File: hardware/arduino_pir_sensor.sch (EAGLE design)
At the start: 43 parts, among them U2 TPS61097-33, U3 BISS0001SO16, U4 NRF24L01+_MODULE, U5 D203S

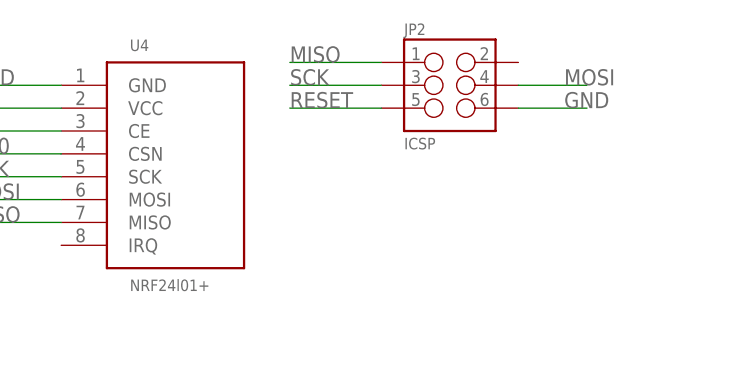
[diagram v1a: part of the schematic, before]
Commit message: - cutout in ground planes on all PCB layers added below wireless module antenna - serial communication connector added
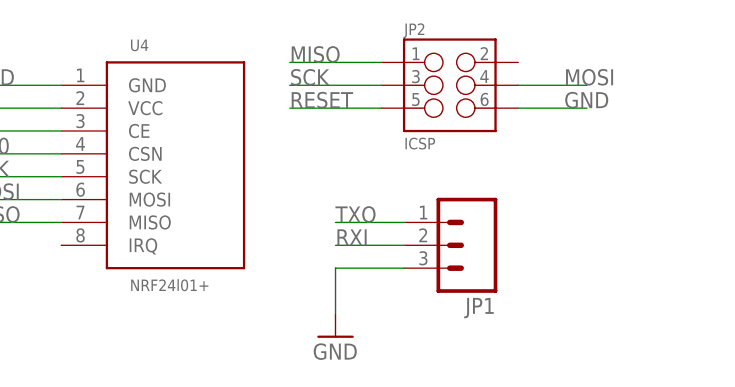
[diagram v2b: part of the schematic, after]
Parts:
- added JP1: (no value), endy-connectors:M03PTH
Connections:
- net GND: now also JP1.3
- net RXI: now also JP1.2
- net TXO: now also JP1.1
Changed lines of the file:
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@@
 <part name="P+8" library="SparkFun" deviceset="3.3V" device="" value="VCC"/>
 <part name="FRAME1" library="SparkFun-Aesthetics" deviceset="FRAME-A3" device=""/>
+<part name="JP1" library="endy-connectors" deviceset="M03" device="PTH"/>
+<part name="GND20" library="SparkFun" deviceset="GND" device=""/>
 </parts>
 <sheets>
@@
 <instance part="P+8" gate="G$1" x="63.5" y="162.56"/>
 <instance part="FRAME1" gate="G$1" x="-142.24" y="-68.58"/>
+<instance part="JP1" gate="G$1" x="185.42" y="17.78" rot="R180"/>
+<instance part="GND20" gate="1" x="170.18" y="7.62"/>
 </instances>
 <busses>
@@
 <pinref part="C16" gate="G$1" pin="P$2"/>
 <wire x1="63.5" y1="142.24" x2="63.5" y2="147.32" width="0.1524" layer="91"/>
+</segment>
+<segment>
+<pinref part="JP1" gate="G$1" pin="3"/>
+<pinref part="GND20" gate="1" pin="GND"/>
+<wire x1="177.8" y1="15.24" x2="170.18" y2="15.24" width="0.1524" layer="91"/>
+<wire x1="170.18" y1="15.24" x2="170.18" y2="10.16" width="0.1524" layer="91"/>
 </segment>
 </net>
@@
 <pinref part="U1" gate="G$1" pin="PD1(TXD)"/>
 </segment>
+<segment>
+<pinref part="JP1" gate="G$1" pin="1"/>
+<wire x1="177.8" y1="20.32" x2="170.18" y2="20.32" width="0.1524" layer="91"/>
+<label x="170.18" y="20.32" size="1.778" layer="95"/>
+</segment>
 </net>
 <net name="D9" class="0">
@@
 <pinref part="U1" gate="G$1" pin="PD0(RXD)"/>
 </segment>
-</net>
+<segment>
+<pinref part="JP1" gate="G$1" pin="2"/>
+<wire x1="177.8" y1="17.78" x2="170.18" y2="17.78" width="0.1524" layer="91"/>
+<label x="170.18" y="17.78" size="1.778" layer="95"/>
+</segment>
+</net>

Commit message: - schematic pdf file updated
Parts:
- JP1: value (none) -> Serial
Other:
- moved on the sheet: JP1, JP2
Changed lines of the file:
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@@
 <part name="P+8" library="SparkFun" deviceset="3.3V" device="" value="VCC"/>
 <part name="FRAME1" library="SparkFun-Aesthetics" deviceset="FRAME-A3" device=""/>
-<part name="JP1" library="endy-connectors" deviceset="M03" device="PTH"/>
+<part name="JP1" library="endy-connectors" deviceset="M03" device="PTH" value="Serial"/>
 <part name="GND20" library="SparkFun" deviceset="GND" device=""/>
 </parts>
@@
 </instance>
 <instance part="P+3" gate="G$1" x="91.44" y="134.62"/>
-<instance part="JP2" gate="G$1" x="182.88" y="35.56">
-<attribute name="OC_NEWARK" x="182.88" y="35.56" size="1.778" layer="96" display="off"/>
-<attribute name="MF" x="182.88" y="35.56" size="1.778" layer="96" display="off"/>
-<attribute name="MPN" x="182.88" y="35.56" size="1.778" layer="96" display="off"/>
+<instance part="JP2" gate="G$1" x="195.58" y="33.02" smashed="yes">
+<attribute name="OC_NEWARK" x="195.58" y="33.02" size="1.778" layer="96" display="off"/>
+<attribute name="MF" x="195.58" y="33.02" size="1.778" layer="96" display="off"/>
+<attribute name="MPN" x="195.58" y="33.02" size="1.778" layer="96" display="off"/>
+<attribute name="NAME" x="190.5" y="38.608" size="1.27" layer="95"/>
+<attribute name="VALUE" x="190.5" y="25.908" size="1.27" layer="96"/>
 </instance>
 <instance part="C2" gate="G$1" x="93.98" y="63.5">
@@
 <instance part="P+8" gate="G$1" x="63.5" y="162.56"/>
 <instance part="FRAME1" gate="G$1" x="-142.24" y="-68.58"/>
-<instance part="JP1" gate="G$1" x="185.42" y="17.78" rot="R180"/>
-<instance part="GND20" gate="1" x="170.18" y="7.62"/>
+<instance part="JP1" gate="G$1" x="194.056" y="13.716" smashed="yes" rot="R180">
+<attribute name="VALUE" x="189.992" y="5.842" size="1.778" layer="96"/>
+<attribute name="NAME" x="188.976" y="19.558" size="1.27" layer="95"/>
+</instance>
+<instance part="GND20" gate="1" x="178.816" y="3.556"/>
 </instances>
 <busses>
@@
 <segment>
 <pinref part="JP2" gate="G$1" pin="6"/>
-<wire x1="198.12" y1="33.02" x2="190.5" y2="33.02" width="0.1524" layer="91"/>
-<label x="195.58" y="33.02" size="1.778" layer="95"/>
+<wire x1="210.82" y1="30.48" x2="203.2" y2="30.48" width="0.1524" layer="91"/>
+<label x="208.28" y="30.48" size="1.778" layer="95"/>
 </segment>
 <segment>
@@
 <pinref part="JP1" gate="G$1" pin="3"/>
 <pinref part="GND20" gate="1" pin="GND"/>
-<wire x1="177.8" y1="15.24" x2="170.18" y2="15.24" width="0.1524" layer="91"/>
-<wire x1="170.18" y1="15.24" x2="170.18" y2="10.16" width="0.1524" layer="91"/>
+<wire x1="186.436" y1="11.176" x2="178.816" y2="11.176" width="0.1524" layer="91"/>
+<wire x1="178.816" y1="11.176" x2="178.816" y2="6.096" width="0.1524" layer="91"/>
 </segment>
 </net>
@@
 <segment>
 <pinref part="JP2" gate="G$1" pin="5"/>
-<wire x1="165.1" y1="33.02" x2="175.26" y2="33.02" width="0.1524" layer="91"/>
-<label x="165.1" y="33.02" size="1.778" layer="95"/>
+<wire x1="177.8" y1="30.48" x2="187.96" y2="30.48" width="0.1524" layer="91"/>
+<label x="177.8" y="30.48" size="1.778" layer="95"/>
 </segment>
 </net>
@@
 <segment>
 <pinref part="JP2" gate="G$1" pin="3"/>
-<wire x1="165.1" y1="35.56" x2="175.26" y2="35.56" width="0.1524" layer="91"/>
-<label x="165.1" y="35.56" size="1.778" layer="95"/>
+<wire x1="177.8" y1="33.02" x2="187.96" y2="33.02" width="0.1524" layer="91"/>
+<label x="177.8" y="33.02" size="1.778" layer="95"/>
 </segment>
 </net>
@@
 <segment>
 <pinref part="JP2" gate="G$1" pin="1"/>
-<wire x1="165.1" y1="38.1" x2="175.26" y2="38.1" width="0.1524" layer="91"/>
-<label x="165.1" y="38.1" size="1.778" layer="95"/>
+<wire x1="177.8" y1="35.56" x2="187.96" y2="35.56" width="0.1524" layer="91"/>
+<label x="177.8" y="35.56" size="1.778" layer="95"/>
 </segment>
 </net>
@@
 <segment>
 <pinref part="JP2" gate="G$1" pin="4"/>
-<wire x1="198.12" y1="35.56" x2="190.5" y2="35.56" width="0.1524" layer="91"/>
-<label x="195.58" y="35.56" size="1.778" layer="95"/>
+<wire x1="210.82" y1="33.02" x2="203.2" y2="33.02" width="0.1524" layer="91"/>
+<label x="208.28" y="33.02" size="1.778" layer="95"/>
 </segment>
 </net>
@@
 <segment>
 <pinref part="JP1" gate="G$1" pin="1"/>
-<wire x1="177.8" y1="20.32" x2="170.18" y2="20.32" width="0.1524" layer="91"/>
-<label x="170.18" y="20.32" size="1.778" layer="95"/>
+<wire x1="186.436" y1="16.256" x2="178.816" y2="16.256" width="0.1524" layer="91"/>
+<label x="178.816" y="16.256" size="1.778" layer="95"/>
 </segment>
 </net>
@@
 <segment>
 <pinref part="JP1" gate="G$1" pin="2"/>
-<wire x1="177.8" y1="17.78" x2="170.18" y2="17.78" width="0.1524" layer="91"/>
-<label x="170.18" y="17.78" size="1.778" layer="95"/>
-</segment>
-</net>
+<wire x1="186.436" y1="13.716" x2="178.816" y2="13.716" width="0.1524" layer="91"/>
+<label x="178.816" y="13.716" size="1.778" layer="95"/>
+</segment>
+</net>

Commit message: - extra power line capacitor added - "connect" button moved away from the mounting screw
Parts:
- added C17: 10uF, SparkFun-Capacitors:CAP1206
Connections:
- net 3.3V: now also C17.1
- net GND: now also C17.2
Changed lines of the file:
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@@
 <part name="JP1" library="endy-connectors" deviceset="M03" device="PTH" value="Serial"/>
 <part name="GND20" library="SparkFun" deviceset="GND" device=""/>
+<part name="C17" library="SparkFun-Capacitors" deviceset="CAP" device="1206" value="10uF">
+<attribute name="MF" value=""/>
+<attribute name="MPN" value=""/>
+<attribute name="OC_NEWARK" value="unknown"/>
+</part>
+<part name="GND21" library="SparkFun" deviceset="GND" device=""/>
+<part name="P+9" library="SparkFun" deviceset="3.3V" device="" value="VCC"/>
 </parts>
 <sheets>
@@
 </instance>
 <instance part="GND20" gate="1" x="178.816" y="3.556"/>
+<instance part="C17" gate="G$1" x="83.82" y="63.5">
+<attribute name="OC_NEWARK" x="83.82" y="63.5" size="1.778" layer="96" display="off"/>
+<attribute name="MF" x="83.82" y="63.5" size="1.778" layer="96" display="off"/>
+<attribute name="MPN" x="83.82" y="63.5" size="1.778" layer="96" display="off"/>
+</instance>
+<instance part="GND21" gate="1" x="83.82" y="55.88"/>
+<instance part="P+9" gate="G$1" x="83.82" y="73.66" smashed="yes">
+<attribute name="VALUE" x="80.264" y="77.216" size="1.778" layer="96"/>
+</instance>
 </instances>
 <busses>
@@
 <wire x1="186.436" y1="11.176" x2="178.816" y2="11.176" width="0.1524" layer="91"/>
 <wire x1="178.816" y1="11.176" x2="178.816" y2="6.096" width="0.1524" layer="91"/>
+</segment>
+<segment>
+<pinref part="GND21" gate="1" pin="GND"/>
+<pinref part="C17" gate="G$1" pin="2"/>
+<wire x1="83.82" y1="58.42" x2="83.82" y2="60.96" width="0.1524" layer="91"/>
 </segment>
 </net>
@@
 <wire x1="63.5" y1="154.94" x2="63.5" y2="162.56" width="0.1524" layer="91"/>
 </segment>
-</net>
+<segment>
+<pinref part="P+9" gate="G$1" pin="3.3V"/>
+<pinref part="C17" gate="G$1" pin="1"/>
+<wire x1="83.82" y1="73.66" x2="83.82" y2="68.58" width="0.1524" layer="91"/>
+</segment>
+</net>

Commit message: change value of the photo cell divider resistor to 47K from 510K
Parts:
- R12: value 510K -> 47K
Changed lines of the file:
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@@
 </part>
 <part name="GND14" library="SparkFun" deviceset="GND" device=""/>
-<part name="R12" library="SparkFun-Resistors" deviceset="RESISTOR" device="0603-RES" value="510K">
+<part name="R12" library="SparkFun-Resistors" deviceset="RESISTOR" device="0603-RES" value="47K">
 <attribute name="MF" value=""/>
 <attribute name="MPN" value=""/>

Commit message: - resistor values fixed
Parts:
- R13: value 2M -> 680K
- R15: value 2M -> 100
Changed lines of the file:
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@@
 <attribute name="OC_NEWARK" value="unknown"/>
 </part>
-<part name="R13" library="SparkFun-Resistors" deviceset="RESISTOR" device="0603-RES" value="2M">
+<part name="R13" library="SparkFun-Resistors" deviceset="RESISTOR" device="0603-RES" value="680K">
 <attribute name="MF" value=""/>
 <attribute name="MPN" value=""/>
@@
 </part>
 <part name="U4" library="modules" deviceset="NRF24L01+_MODULE" device=""/>
-<part name="R15" library="SparkFun-Resistors" deviceset="RESISTOR" device="0603-RES" value="2M">
+<part name="R15" library="SparkFun-Resistors" deviceset="RESISTOR" device="0603-RES" value="100">
 <attribute name="MF" value=""/>
 <attribute name="MPN" value=""/>
